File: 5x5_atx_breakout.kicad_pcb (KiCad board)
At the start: 2 copper layers, 50 x 50 mm, 43 parts, among them P1 CONN_10X2, P2 CONN_1, P3 CONN_1, P4 CONN_1, P5 CONN_1, P6 CONN_1, P7 CONN_1, SW1 SWITCH_INV, SW2 SWITCH_INV, SW3 SWITCH_INV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

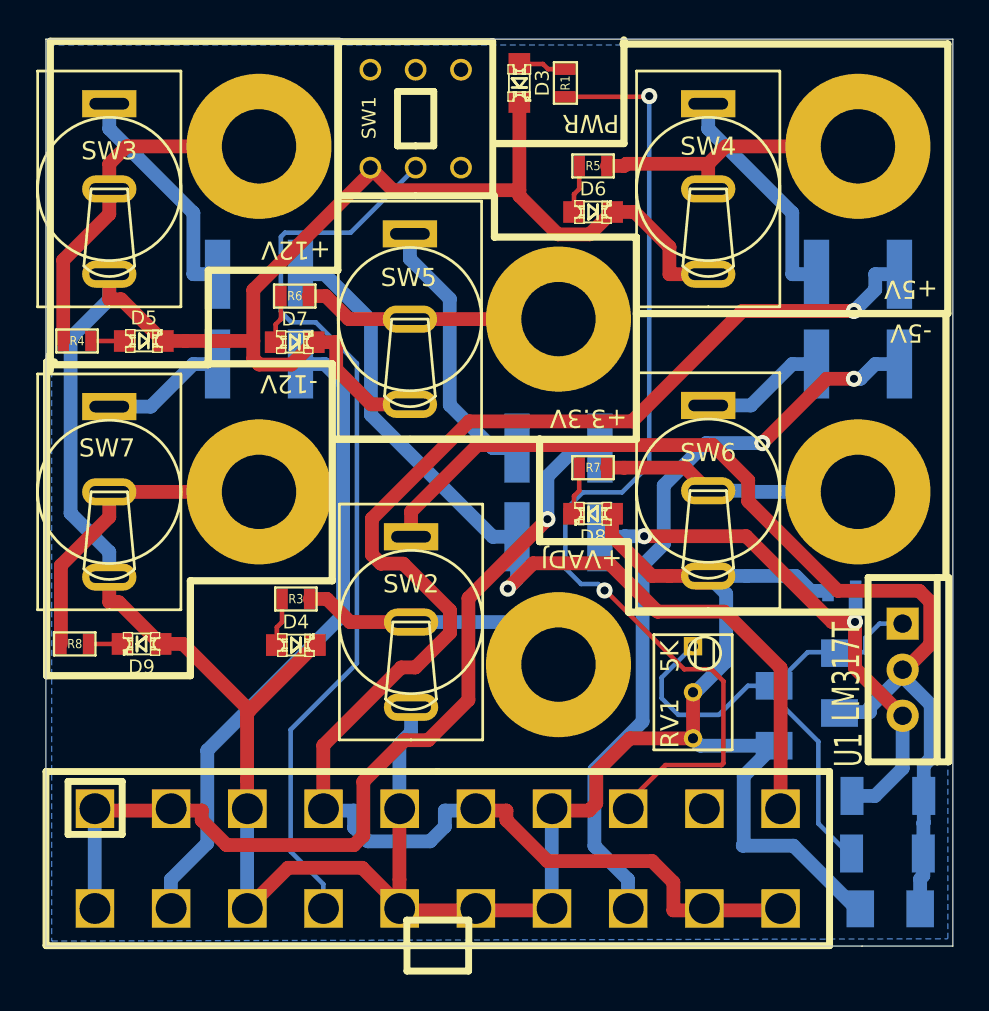
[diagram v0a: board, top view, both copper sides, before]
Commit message: standardized the pcb text thickness to 0.25mm for title, usage info,... and 0.125mm (dirtypcbs.com minimum) for other stuff and moved text so that references is not hidden by components
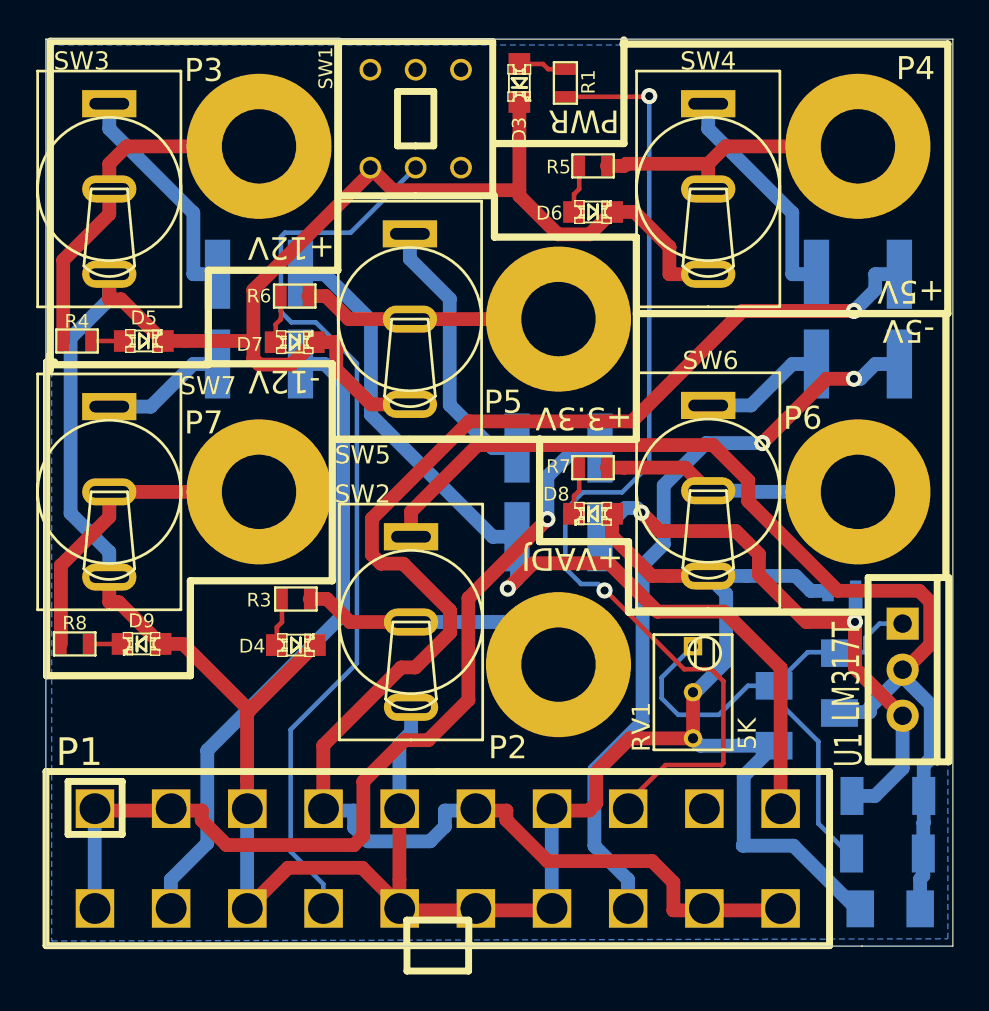
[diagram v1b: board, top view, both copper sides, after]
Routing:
- net +VADJ_IN: track 30.3 -> 32.4 mm
